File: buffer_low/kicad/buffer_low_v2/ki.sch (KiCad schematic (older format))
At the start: 46 parts, among them J1 Header-2, J1 Header_M1x02, J1 J3, J2 Header-3, J2 Screw_TermB_01x03, J21 BNC, J23 TermBlk_2, J3 Header-2, J3 Header_M1x02, J3 J3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

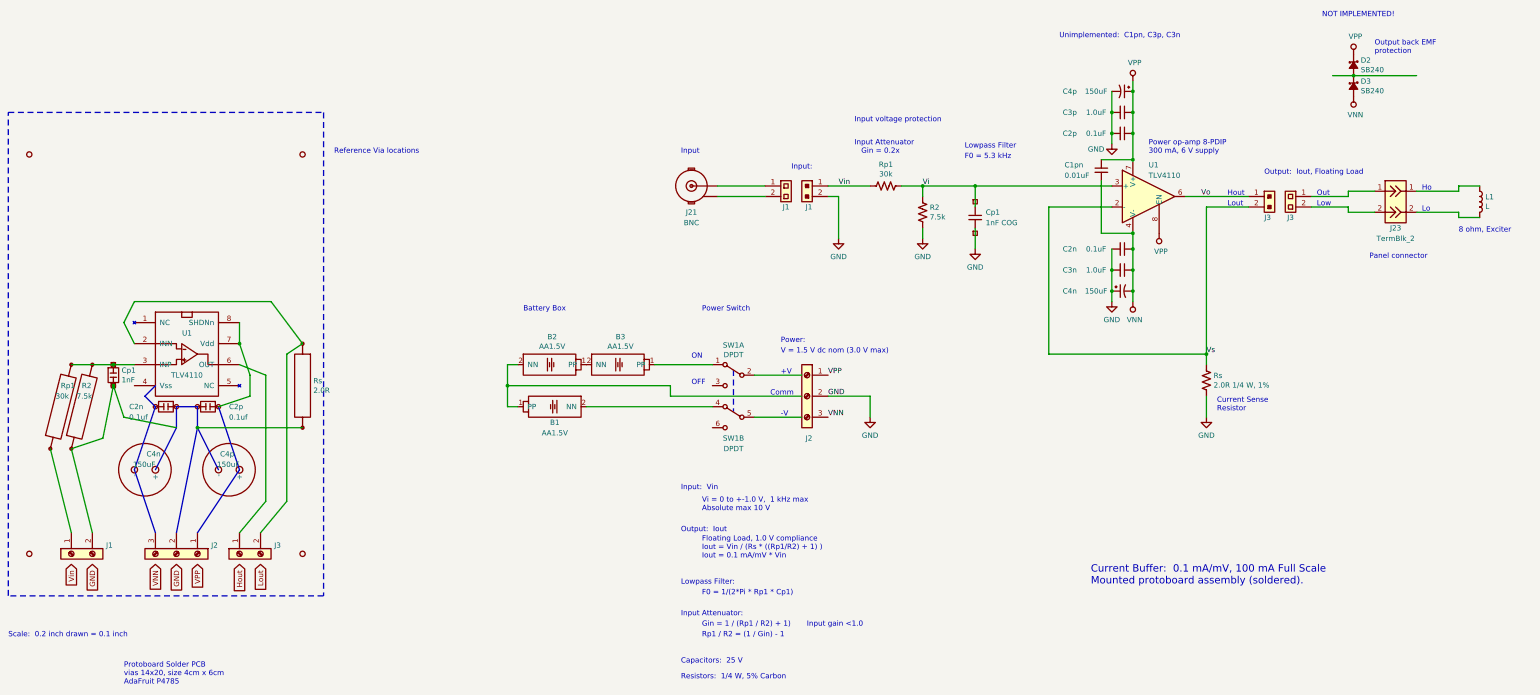
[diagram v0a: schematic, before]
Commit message: buffer_low:  Schematic buffer_low_v2/ v2.0.1 2023-12-27
    Battery change to +-3 V (4 cells).
    Protoboard layout revised to as-built.
    Add wire colors.
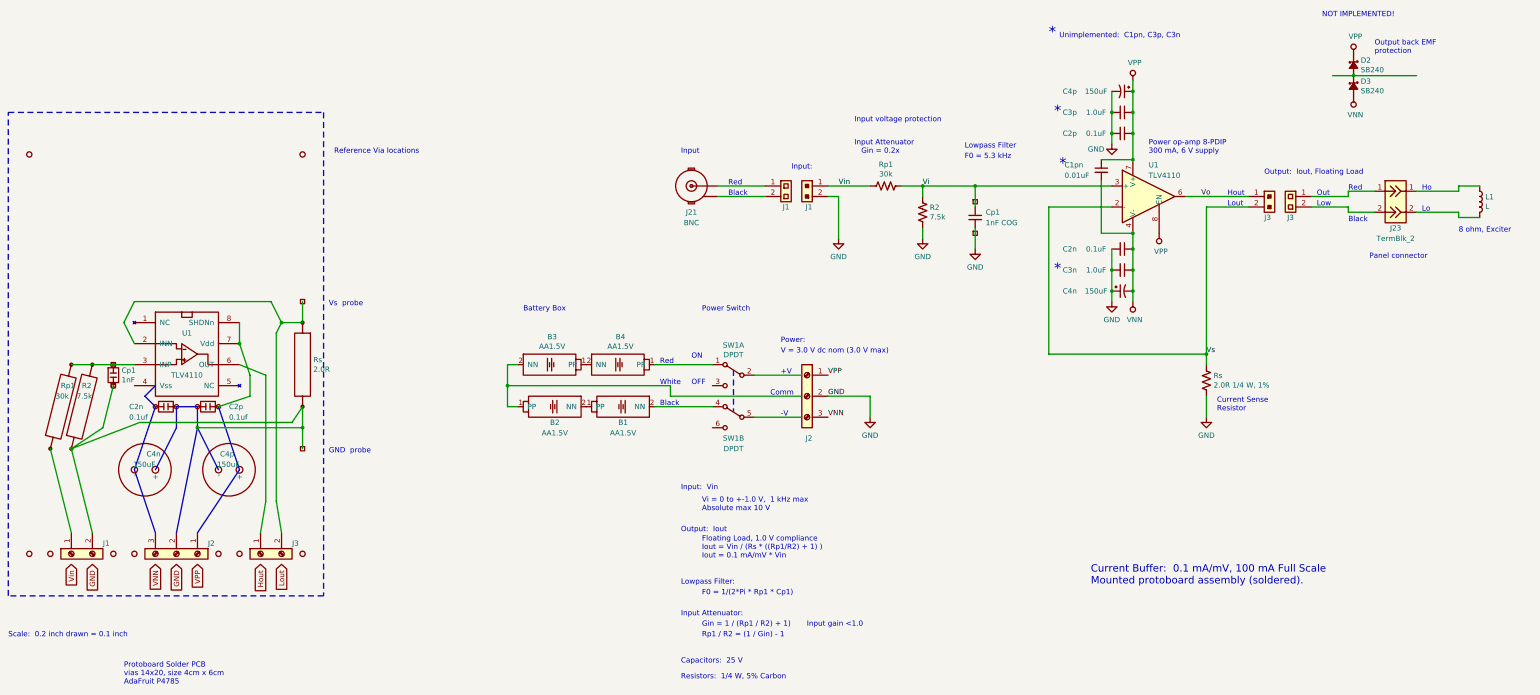
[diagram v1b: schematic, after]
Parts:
- added B1: AA1.5V, symbol _Local:Battery
- added J? (x2): Socket1, symbol _Local:Socket1
- added P? (x5): Pin, symbol _Breadboard:Pin
- renumbered B1 to B2, B2 to B3, B3 to B4
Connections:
- wire segments 87 -> 92
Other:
- note added: "*"
- note added: "Black"
- note added: "GND probe"
- note added: "Red"
- note added: "V = 3.0 V dc nom (3.0 V max)"
- note added: "Vs probe"
- note added: "White"
- note removed: "V = 1.5 V dc nom (3.0 V max)"
- moved on the sheet: J3, Rs
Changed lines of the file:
@@
 Sheet 1 1
 Title "Low-Current Buffer - buffer_low_v2/"
-Date "2023-11-17"
-Rev "v2.0.0"
+Date "2023-12-27"
+Rev "v2.0.1"
 Comp "William A. Hudson"
-Comment1 ""
+Comment1 "v2.0.1  +-3 V battery, protoboard layout, wire colors"
 Comment2 ""
 Comment3 ""
@@
 -V
 Text Notes 9350 6900 0    50   ~ 0
-V = 1.5 V dc nom (3.0 V max)
+V = 3.0 V dc nom (3.0 V max)
 Wire Wire Line
 	13400 7300 13400 7500
@@
 Text GLabel 3400 8900 3    50   Input ~ 0
 VNN
-Text GLabel 4200 8900 3    50   Input ~ 0
+Text GLabel 4400 8900 3    50   Input ~ 0
 Hout
 Text GLabel 3800 8900 3    50   Input ~ 0
 VPP
-Text GLabel 4400 8900 3    50   Input ~ 0
+Text GLabel 4600 8900 3    50   Input ~ 0
 Lout
 Text GLabel 2800 8900 3    50   Input ~ 0
@@
 L _Local:Screw_TermB_01x02 J3
 U 1 1 6559CDAF
-P 4200 8800
-F 0 "J3" V 4119 8470 50  0000 R CNN
-F 1 "Header-2" V 4075 8470 50  0001 R CNN
-F 2 "" H 4200 8800 50  0001 C CNN
-F 3 "" H 4200 8800 50  0001 C CNN
-	1    4200 8800
+P 4400 8800
+F 0 "J3" V 4300 8500 50  0000 R CNN
+F 1 "Header-2" V 4275 8470 50  0001 R CNN
+F 2 "" H 4400 8800 50  0001 C CNN
+F 3 "" H 4400 8800 50  0001 C CNN
+	1    4400 8800
 	0    -1   1    0
 $EndComp
@@
 U 1 1 6559CEA8
 P 3800 8800
-F 0 "J2" V 3719 8930 50  0000 L CNN
+F 0 "J2" V 3700 8900 50  0000 L CNN
 F 1 "Header-3" V 3764 8930 50  0001 L CNN
 F 2 "" H 3800 8600 50  0001 C CNN
@@
 U 1 1 6559F54F
 P 2600 8800
-F 0 "J1" V 2519 8470 50  0000 R CNN
+F 0 "J1" V 2500 8500 50  0000 R CNN
 F 1 "Header-2" V 2475 8470 50  0001 R CNN
 F 2 "" H 2600 8800 50  0001 C CNN
@@
 L _Breadboard:R4_4_0 Rs
 U 1 1 6559FA4A
-P 4800 7200
-F 0 "Rs" H 4697 7154 50  0000 R CNN
-F 1 "2.0R" H 4697 7245 50  0000 R CNN
-F 2 "" H 4800 7200 50  0001 C CNN
-F 3 "" H 4800 7200 50  0001 C CNN
-	1    4800 7200
+P 4800 7000
+F 0 "Rs" H 4697 6954 50  0000 R CNN
+F 1 "2.0R" H 4697 7045 50  0000 R CNN
+F 2 "" H 4800 7000 50  0001 C CNN
+F 3 "" H 4800 7000 50  0001 C CNN
+	1    4800 7000
 	-1   0    0    1
 $EndComp
 $Comp
-L _Local:Battery B3
+L _Local:Battery B4
 U 1 1 655A6D94
 P 7800 7000
-F 0 "B3" H 7825 7265 50  0000 C CNN
+F 0 "B4" H 7825 7265 50  0000 C CNN
 F 1 "AA1.5V" H 7825 7174 50  0000 C CNN
 F 2 "" H 7800 7000 50  0001 C CNN
@@
 $EndComp
 $Comp
-L _Local:Battery B2
+L _Local:Battery B3
 U 1 1 655A7184
 P 7150 7000
-F 0 "B2" H 7175 7265 50  0000 C CNN
+F 0 "B3" H 7175 7265 50  0000 C CNN
 F 1 "AA1.5V" H 7175 7174 50  0000 C CNN
 F 2 "" H 7150 7000 50  0001 C CNN
@@
 $EndComp
 $Comp
-L _Local:Battery B1
+L _Local:Battery B2
 U 1 1 655A723D
 P 7200 7400
-F 0 "B1" H 7200 7250 50  0000 C CNN
+F 0 "B2" H 7200 7250 50  0000 C CNN
 F 1 "AA1.5V" H 7200 7150 50  0000 C CNN
 F 2 "" H 7200 7400 50  0001 C CNN
@@
 Wire Wire Line
 	6750 7400 6850 7400
-Wire Wire Line
-	8700 7400 7500 7400
 $Comp
 L Switch:SW_DPDT_x2 SW1
@@
 	4000 7400 4200 8000
 Wire Wire Line
-	3800 7600 4800 7600
-Wire Wire Line
 	4200 7000 4450 7100
 Wire Wire Line
 	4450 7100 4450 8300
 Wire Wire Line
-	4450 8300 4200 8600
-Wire Wire Line
-	4400 8600 4650 8300
-Wire Wire Line
-	4650 8300 4650 6900
-Wire Wire Line
-	4650 6900 4800 6800
+	4450 8300 4400 8600
+Wire Wire Line
+	4600 8600 4550 8300
+Wire Wire Line
+	4550 8300 4550 6700
 Wire Wire Line
 	2400 7800 2600 8600
@@
 Wire Bus Line
 	3600 7400 3800 7400
-Wire Bus Line
-	3800 7400 3800 7600
-Wire Wire Line
-	2600 7800 2900 7700
-Wire Wire Line
-	2900 7700 3000 7200
-Wire Wire Line
-	3000 7200 3100 7500
-Wire Wire Line
-	3100 7500 3600 7600
-Connection ~ 3000 7200
+Wire Wire Line
+	2600 7800 2900 7600
 Wire Bus Line
 	3600 8600 3800 7600
@@
 Wire Bus Line
 	4000 8000 3800 7600
-Connection ~ 3800 7600
 Wire Wire Line
 	3200 6800 3100 6600
 Wire Wire Line
 	3100 6600 3200 6400
-Wire Wire Line
-	3200 6400 4500 6400
-Wire Wire Line
-	4500 6400 4800 6800
 Wire Notes Line
 	2000 9200 2000 4600
@@
 Text Notes 5100 5000 0    50   ~ 0
 Reference Via locations
+Wire Wire Line
+	2900 7600 3000 7200
+Wire Wire Line
+	4550 6700 4600 6600
+Wire Wire Line
+	4600 6600 4800 6600
+$Comp
+L _Local:Socket1 J?
+U 1 1 658C4757
+P 4800 6400
+F 0 "J?" H 4848 6446 50  0001 L CNN
+F 1 "Socket1" H 4848 6355 50  0001 L CNN
+F 2 "" H 4800 6400 50  0001 C CNN
+F 3 "" H 4800 6400 50  0001 C CNN
+	1    4800 6400
+	1    0    0    -1
+$EndComp
+$Comp
+L _Local:Socket1 J?
+U 1 1 658C4C48
+P 4800 7800
+F 0 "J?" H 4848 7846 50  0001 L CNN
+F 1 "Socket1" H 4848 7755 50  0001 L CNN
+F 2 "" H 4800 7800 50  0001 C CNN
+F 3 "" H 4800 7800 50  0001 C CNN
+	1    4800 7800
+	1    0    0    -1
+$EndComp
+Wire Wire Line
+	4800 6400 4800 6600
+Text Notes 5050 7850 0    50   ~ 0
+GND  probe
+Text Notes 5050 6450 0    50   ~ 0
+Vs  probe
+Wire Wire Line
+	3200 6400 4500 6400
+Wire Wire Line
+	4600 6600 4500 6400
+Connection ~ 4600 6600
+Wire Bus Line
+	3800 7400 3800 7600
+Wire Wire Line
+	4800 7400 4800 7600
+Wire Wire Line
+	3800 7600 4800 7600
+Connection ~ 3800 7600
+Connection ~ 4800 7600
+Wire Wire Line
+	4800 7600 4800 7800
+Wire Wire Line
+	2600 7800 3250 7550
+Wire Wire Line
+	3250 7550 4700 7550
+Wire Wire Line
+	4700 7550 4800 7400
+Connection ~ 2600 7800
+$Comp
+L _Breadboard:Pin P?
+U 1 1 658F6B05
+P 2400 8800
+F 0 "P?" H 2453 8846 50  0001 L CNN
+F 1 "Pin" H 2453 8755 50  0001 L CNN
+F 2 "" H 2400 8800 50  0001 C CNN
+F 3 "" H 2400 8800 50  0001 C CNN
+	1    2400 8800
+	1    0    0    -1
+$EndComp
+$Comp
+L _Breadboard:Pin P?
+U 1 1 658F6B85
+P 3000 8800
+F 0 "P?" H 3053 8846 50  0001 L CNN
+F 1 "Pin" H 3053 8755 50  0001 L CNN
+F 2 "" H 3000 8800 50  0001 C CNN
+F 3 "" H 3000 8800 50  0001 C CNN
+	1    3000 8800
+	1    0    0    -1
+$EndComp
+$Comp
+L _Breadboard:Pin P?
+U 1 1 658F6C05
+P 3200 8800
+F 0 "P?" H 3253 8846 50  0001 L CNN
+F 1 "Pin" H 3253 8755 50  0001 L CNN
+F 2 "" H 3200 8800 50  0001 C CNN
+F 3 "" H 3200 8800 50  0001 C CNN
+	1    3200 8800
+	1    0    0    -1
+$EndComp
+$Comp
+L _Breadboard:Pin P?
+U 1 1 658F6CAC
+P 4000 8800
+F 0 "P?" H 4053 8846 50  0001 L CNN
+F 1 "Pin" H 4053 8755 50  0001 L CNN
+F 2 "" H 4000 8800 50  0001 C CNN
+F 3 "" H 4000 8800 50  0001 C CNN
+	1    4000 8800
+	1    0    0    -1
+$EndComp
+$Comp
+L _Breadboard:Pin P?
+U 1 1 658F6D2C
+P 4200 8800
+F 0 "P?" H 4253 8846 50  0001 L CNN
+F 1 "Pin" H 4253 8755 50  0001 L CNN
+F 2 "" H 4200 8800 50  0001 C CNN
+F 3 "" H 4200 8800 50  0001 C CNN
+	1    4200 8800
+	1    0    0    -1
+$EndComp
+$Comp
+L _Local:Battery B1
+U 1 1 658F90CB
+P 7850 7400
+F 0 "B1" H 7850 7250 50  0000 C CNN
+F 1 "AA1.5V" H 7850 7150 50  0000 C CNN
+F 2 "" H 7850 7400 50  0001 C CNN
+F 3 "" H 7850 7400 50  0001 C CNN
+	1    7850 7400
+	-1   0    0    -1
+$EndComp
+Wire Wire Line
+	8150 7400 8700 7400
+Text Notes 11950 4650 0    100  ~ 0
+*
+Text Notes 12000 5150 0    100  ~ 0
+*
+Text Notes 11950 6150 0    100  ~ 0
+*
+Text Notes 11900 3900 0    100  ~ 0
+*
+Text Notes 8200 7000 0    50   ~ 0
+Red
+Text Notes 8200 7400 0    50   ~ 0
+Black
+Text Notes 8200 7200 0    50   ~ 0
+White
+Text Notes 8850 5300 0    50   ~ 0
+Red
+Text Notes 8850 5400 0    50   ~ 0
+Black
+Text Notes 14750 5350 0    50   ~ 0
+Red
+Text Notes 14750 5650 0    50   ~ 0
+Black
 $EndSCHEMATC
